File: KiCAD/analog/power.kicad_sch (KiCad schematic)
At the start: 0 parts

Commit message: KiCad revC: ±12V subsystem validated — LT1054 Fig-15 inverter + LM2940 LDO
Converged after iterating in LTspice:

* New standalone power project (KiCAD/power/) proves the topology before
  surgery on the analog project's power sheet. LT1054 as regulated inverter
  (not Figure 22 doubler — doubler was abandoned when single-FB-loop couldn't
  regulate both rails symmetrically). LM2940CT-12 LDO handles +12V from the
  13.8V bus. Both rails measure ±11.93V in sim at 1K load, VREF holds flat
  at 2.5V, V(FB_SD) settles at 0.596V.

* Datasheet-compliant divider values after discovering R16=10K violated the
  VREF ±100µA current limit: R16=20K, R17=240K (empirically tuned, differs
  from both my circuit analysis and datasheet formula — LTspice LT1054 model
  uses ~0.6V internal reference instead of the datasheet's 1.21V).
  C18=2.2nF loop comp matches datasheet "2 nF for all output voltages".

* New LM2940CT-12 symbol in xmitter.kicad_sym (TO-220-3, drop-in replacement
  for LM7812 pinout, 0.5V dropout vs 7812's 2V — needed for 13.8V-to-12V
  with headroom to spare).

* LTspice validation files in Documentation/:
    - power_sim.cir  (hand-written netlist, works in LTspice via File→Open)
    - power_sim.asc  (initial schematic attempt, retained as reference —
                      geometry is messy, use .cir instead)
    - Draft3.asc     (scratch for inspecting LT1054 symbol pin order)

Next step: migrate the validated topology into KiCAD/analog/power.kicad_sch,
replacing the shelved tube-era regulators (U15 LM317L, U19 LM7812, U23
LT1054) and the removed bridge rectifier that fed them.

Co-Authored-By: Claude Opus 4.7 <noreply@anthropic.com>
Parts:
- added C108: 220nF, Capacitor_THT:C_Disc_D6.0mm_W2.5mm_P5.00mm, symbol Device:C_US
- added C109: 0.47uF, Capacitor_THT:C_Rect_L7.0mm_W3.5mm_P5.00mm, symbol Device:C
- added C11: 10uF, symbol Device:C_Polarized_US
- added C110: 0.1uF, Capacitor_THT:C_Disc_D5.0mm_W2.5mm_P5.00mm, symbol Device:C
- added C111: 22uF, Capacitor_THT:CP_Radial_D5.0mm_P2.00mm, symbol Device:C_Polarized
- added C12: C_US, symbol Device:C_US
- added C13: 100uF, symbol Device:C_Polarized_US
- added C16: 0.001uF, symbol Device:C
- added J3: Screw_Terminal_01x02, symbol Connector:Screw_Terminal_01x02
- added R14: 10K, symbol Device:R_US
- added R15: 82K for -11.1V, 91K for -12.0V, symbol Device:R_US
- added U6: LT1054, symbol Regulator_SwitchedCapacitor:LT1054
- added U8: LM2940CT-12, Package_TO_SOT_THT:TO-220-3_Vertical, symbol xmitter:LM2940CT-12
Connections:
- new net: C108.1, C109.1, C12.1, J3.2 (Pin_2), U6.8 (V+), U8.1 (VI)
- new net: R14.1, U6.1 (FB/SHDN)
- new net: C16.2, R14.2, R15.1, U6.6 (VREF)
- new net: C11.1, U6.2 (CAP+)
- new net: C11.2, U6.4 (CAP-)
- new net +12V: C110.1, C111.1, U8.3 (VO)
- new net -12V: C13.2, C16.1, R15.2, U6.5 (-VOUT)
- new net GND: C108.2, C109.2, C110.2, C111.2, C12.2, C13.1, J3.1 (Pin_1), U6.3 (GND), U8.2 (GND)
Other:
- note added: "13.8V in"
- note added: "C105"

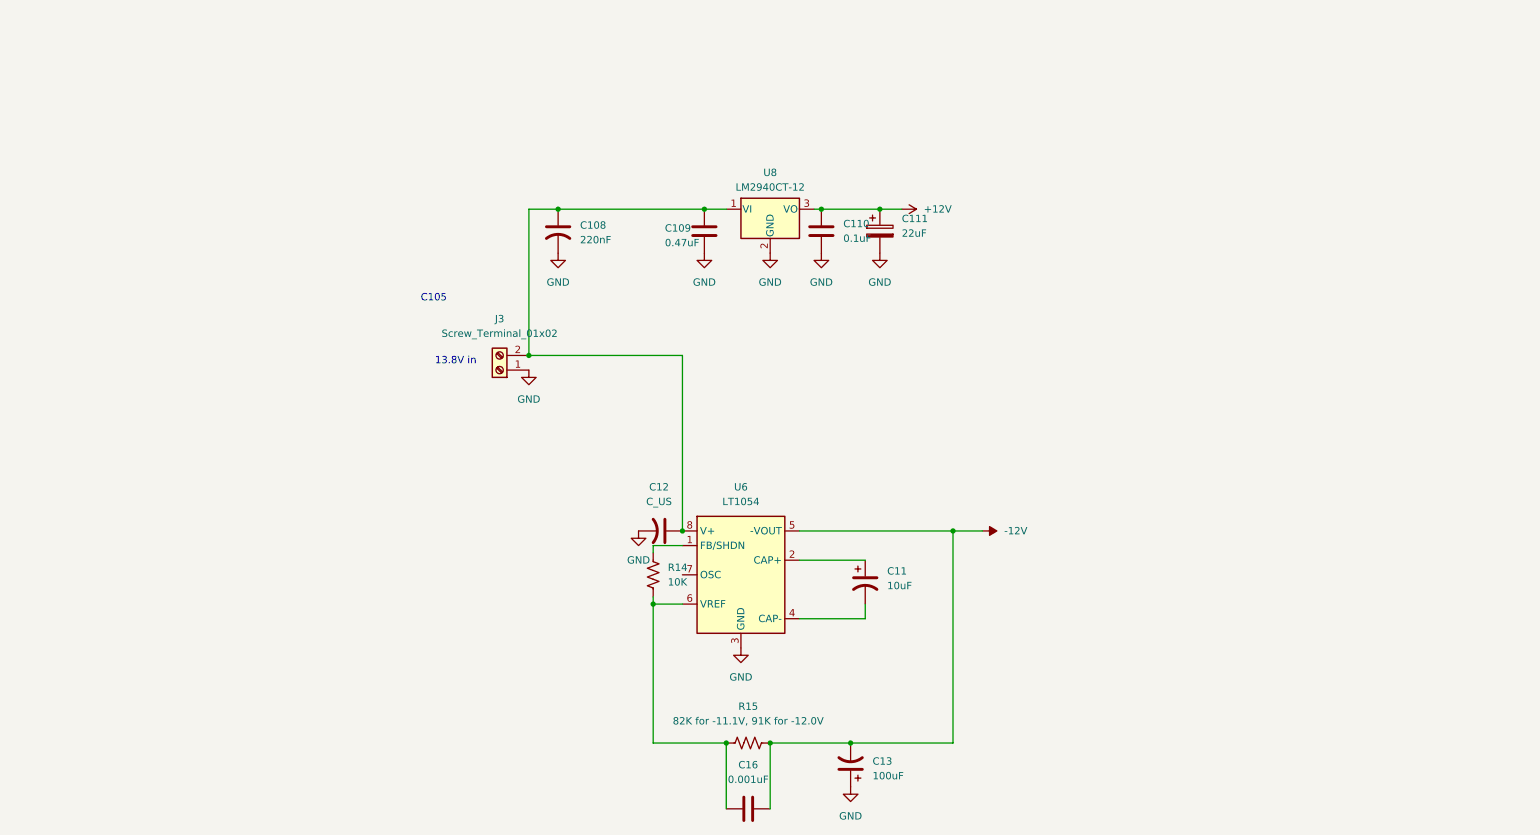
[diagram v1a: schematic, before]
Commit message: KiCad revC: LM2940CT-5.0 symbol + ±12V subsystem migrated into analog/power
* xmitter.kicad_sym: new LM2940CT-5.0 symbol, pin-compat with 7805 (same
  TO-220 topology as the LM2940CT-12 added last commit). For the +5V rail
  feeding the Metro.

* analog/power.kicad_sch: substantial migration of the validated ±12V
  subsystem (LT1054 regulated inverter + LM2940CT-12 LDO) from the
  standalone KiCAD/power/ project.  Tube-era regulators (LM317L, LM7812,
  original LT1054 attempt) and bridge rectifier gone. Values still need
  final cleanup (R14=10K->20K, R15 string->240K, C16=1n->2.2n, C12 no
  value) before next sim validation.

* Not pushing yet — 28V relay doubler stage will land in the same sheet
  before this gets published.

Co-Authored-By: Claude Opus 4.7 <noreply@anthropic.com>
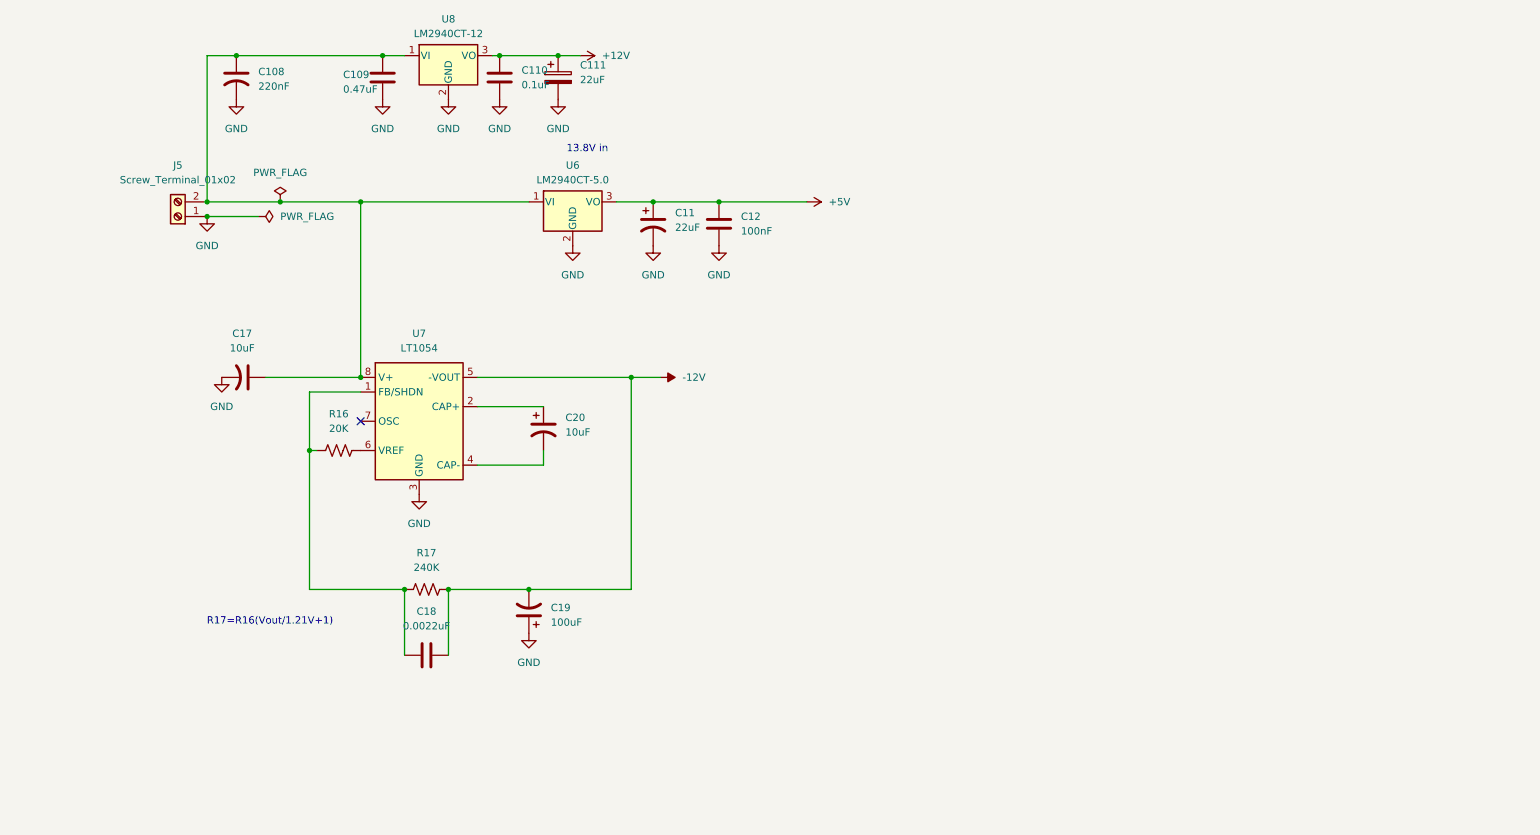
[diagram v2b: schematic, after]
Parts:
- removed C12: C_US, symbol Device:C_US
- removed C13: 100uF, symbol Device:C_Polarized_US
- removed C16: 0.001uF, symbol Device:C
- removed J3: Screw_Terminal_01x02, symbol Connector:Screw_Terminal_01x02
- removed R14: 10K, symbol Device:R_US
- removed R15: 82K for -11.1V, 91K for -12.0V, symbol Device:R_US
- removed U6: LT1054, symbol Regulator_SwitchedCapacitor:LT1054
- added C12: 100nF, symbol Device:C
- added C17: 10uF, symbol Device:C_US
- added C18: 0.0022uF, symbol Device:C
- added C19: 100uF, symbol Device:C_Polarized_US
- added C20: 10uF, symbol Device:C_Polarized_US
- added J5: Screw_Terminal_01x02, symbol Connector:Screw_Terminal_01x02
- added R16: 20K, symbol Device:R_US
- added R17: 240K, symbol Device:R_US
- added U6: LM2940CT-5.0, Package_TO_SOT_THT:TO-220-3_Vertical, symbol xmitter:LM2940CT-5.0
- added U7: LT1054, symbol Regulator_SwitchedCapacitor:LT1054
- C11: value 10uF -> 22uF
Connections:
- net -12V: now also C18.1, C19.2, R17.2, U7.5 (-VOUT)
- net GND: now also C11.2, C12.2, C17.2, C19.1, J5.1 (Pin_1), U6.2 (GND), U7.3 (GND)
- net at C108.1, C109.1, U8.1 (VI): now also C17.1, J5.2 (Pin_2), U6.1 (VI), U7.8 (V+)
- net +5V: now reaches C11.1
- net +5V: now also C12.1, U6.3 (VO)
- new net: C18.2, R16.1, R17.1, U7.1 (FB/SHDN)
- new net: C20.1, U7.2 (CAP+)
- new net: C20.2, U7.4 (CAP-)
- new net: R16.2, U7.6 (VREF)
- no-connect marks 0 -> 1
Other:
- note added: "R17=R16(Vout/1.21V+1)"
- note removed: "C105"

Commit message: KiCad revC: +28V doubler + 5V LDO added to analog/power, ERC clean
- Migrated LT1054 Figure 20 positive doubler from standalone power project
  into analog/power.kicad_sch for the +28V reed-relay rail
- Added LM2940CT-5.0 LDO stage for Metro / Si5351 +5V rail
- analog ERC: 4 messages, all classified as false positives (U9 pin 5
  tied to GND per Fig 20 topology, PCF_P5_SPARE intentionally unused,
  VIN pins now driven by added +5V rail)
- Added QRP Labs 10W PA / 5W PA reference PDFs + 2N7000 + lm2940c
  datasheets to Documentation/QRP_Examples/

Co-Authored-By: Claude Opus 4.7 <noreply@anthropic.com>
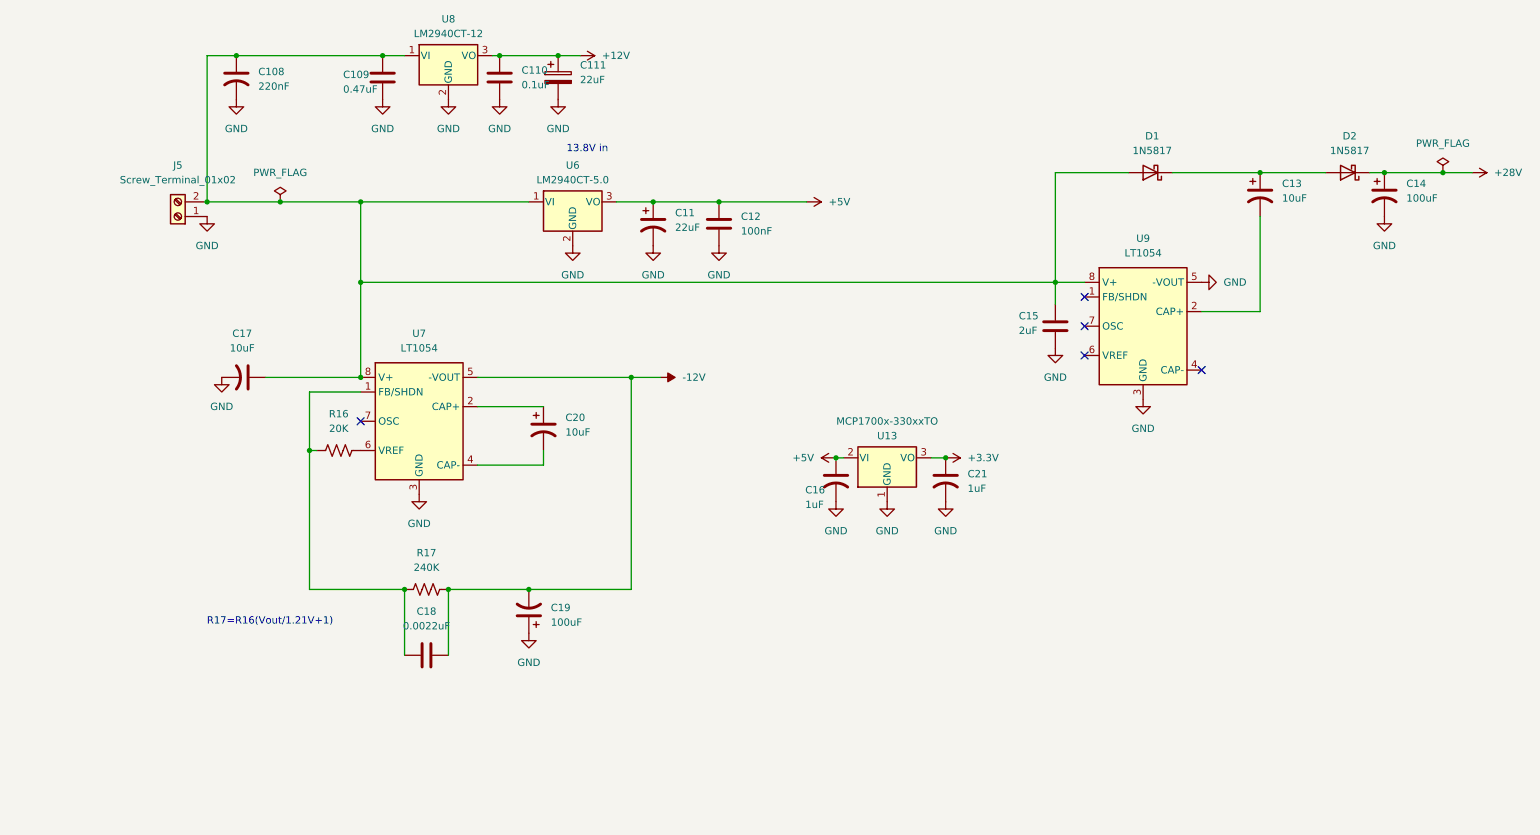
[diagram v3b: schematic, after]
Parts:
- added C13: 10uF, symbol Device:C_Polarized_US
- added C14: 100uF, symbol Device:C_Polarized_US
- added C15: 2uF, symbol Device:C
- added C16, C21: 1uF, Capacitor_THT:C_Rect_L7.2mm_W4.5mm_P5.00mm, symbol Device:C_US
- added D1, D2: 1N5817, Diode_THT:D_DO-41_SOD81_P10.16mm_Horizontal, symbol Diode:1N5817
- added U13: MCP1700x-330xxTO, Package_TO_SOT_THT:TO-92_Inline_Wide, symbol Regulator_Linear:MCP1700x-330xxTO
- added U9: LT1054, symbol Regulator_SwitchedCapacitor:LT1054
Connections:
- net +5V: now also C16.1, U13.2 (VI)
- net GND: now also C14.2, C15.2, C16.2, C21.2, U13.1 (GND), U9.3 (GND), U9.5 (-VOUT)
- net at C108.1, C109.1, C17.1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: now also C15.1, D1.2 (A), U9.8 (V+)
- new net: C13.1, D1.1 (K), D2.2 (A)
- new net: C13.2, U9.2 (CAP+)
- new net +28V: C14.1, D2.1 (K)
- new net +3.3V: C21.1, U13.3 (VO)
- no-connect marks 1 -> 5

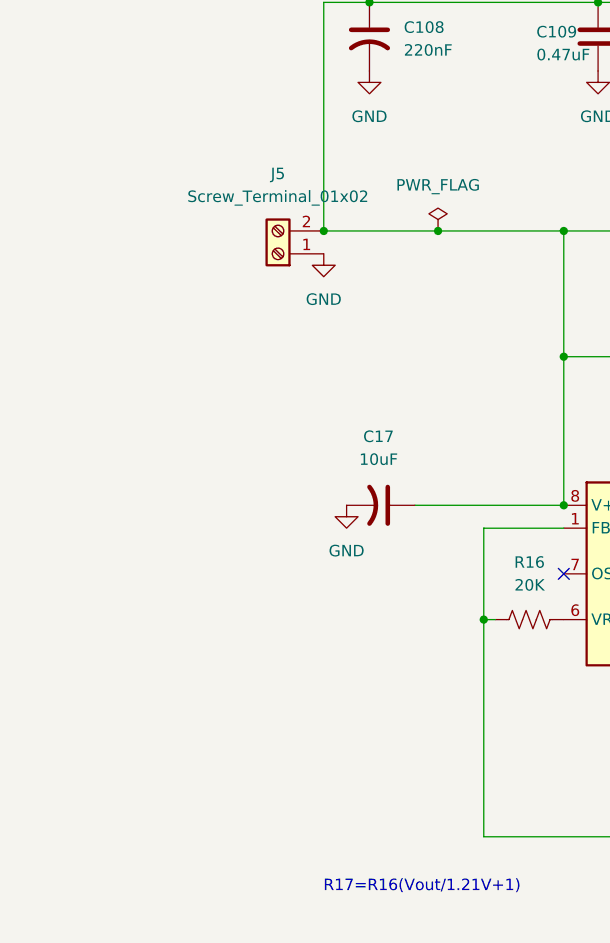
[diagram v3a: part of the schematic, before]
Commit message: KiCad revC: heartbeat-triggered SS PA power disconnect + flyback diodes
analog/power.kicad_sch:
- Added K6 (RLP20-12L10MS2F SPST-NO relay, 10A @ 30V DC contacts,
  12V/20mA coil) in series between +13.8V shack supply and J33
  (new 2-pin screw terminal supplying ss_pa board)
- K6 coil driven by existing Q5+Q7 series safety cascade on
  SS_PWR_RLY net: both Q5 (firmware control via PCF8575 P14) AND
  Q7 (CD14538B heartbeat watchdog Q_A) must be ON for the relay
  to energize. Firmware disable or heartbeat failure cuts PA power.
- Added 90R series resistor in the coil leg to drop +13.8V rail
  down to the 12V coil's nominal operating voltage
- Added D4 (1N4001 flyback diode) across K6 coil, cathode on +13.8V
  side, anode on SS_PWR_RLY (Q5 drain) side
- J7 (tube-era HV primary screw terminal) remains on the SS_PWR_RLY
  net so a future external tube-PA HV relay would share the same
  safety chain

ss_pa/pa_stage.kicad_sch:
- Added D2 (1N5822 Schottky, 3A/40V) flyback diode across L5. When
  the heartbeat relay opens with current flowing through L5, the
  12 uH inductor's stored energy (up to ~13 uJ at 1.5A) would
  otherwise swing the relay-side node hundreds of volts negative
  and arc the K6 contacts. D2 clamps that swing to ~V_f below the
  C6-held +13.8V bus.
- D2 polarity: cathode (pin 1) on J2/relay side, anode (pin 2) on
  +13.8V bus side.

Both netlists re-exported.

Co-Authored-By: Claude Opus 4.7 <noreply@anthropic.com>
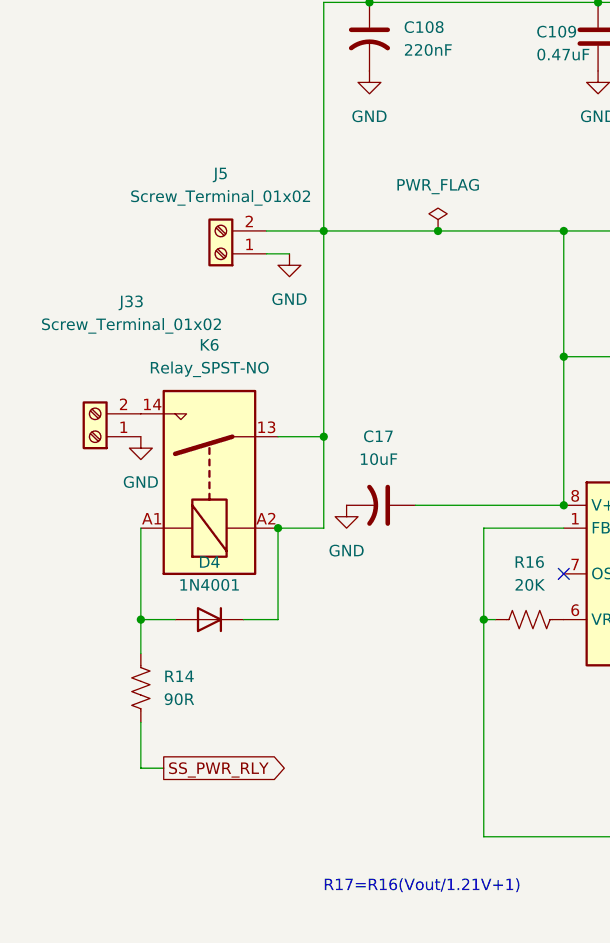
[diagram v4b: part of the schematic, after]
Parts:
- added D4: 1N4001, Diode_THT:D_DO-41_SOD81_P10.16mm_Horizontal, symbol Diode:1N4001
- added J33: Screw_Terminal_01x02, symbol Connector:Screw_Terminal_01x02
- added K6: Relay_SPST-NO, symbol Relay:Relay_SPST-NO
- added R14: 90R, symbol Device:R_US
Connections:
- net GND: now also J33.1 (Pin_1)
- net at C108.1, C109.1, C15.1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: now also D4.1 (K), K6.13, K6.A2
- new net: D4.2 (A), K6.A1, R14.1
- new net: J33.2 (Pin_2), K6.14
- new net SS_PWR_RLY: R14.2
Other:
- moved on the sheet: J5

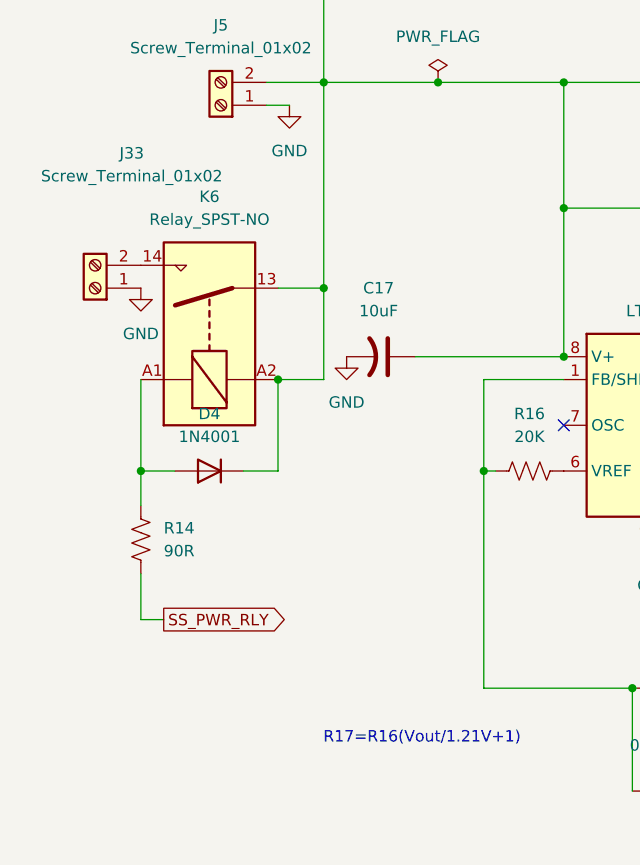
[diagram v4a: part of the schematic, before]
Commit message: KiCad revC: analog R6 -> 0R jumper (ENC_INT line)
Protoshield already has R7 (330R) + R8 (10K pullup) at the Metro
GPIO input, which is the right place for ESD/noise conditioning
(closest to the sensitive pin). R6 on analog was a duplicate series
resistor on the same signal; dropping it to 0R turns it into an
in-the-path jumper without having to rename the ENC_INT_CLEAN /
ENC_INT labels on multiple sheets.

Co-Authored-By: Claude Opus 4.7 <noreply@anthropic.com>
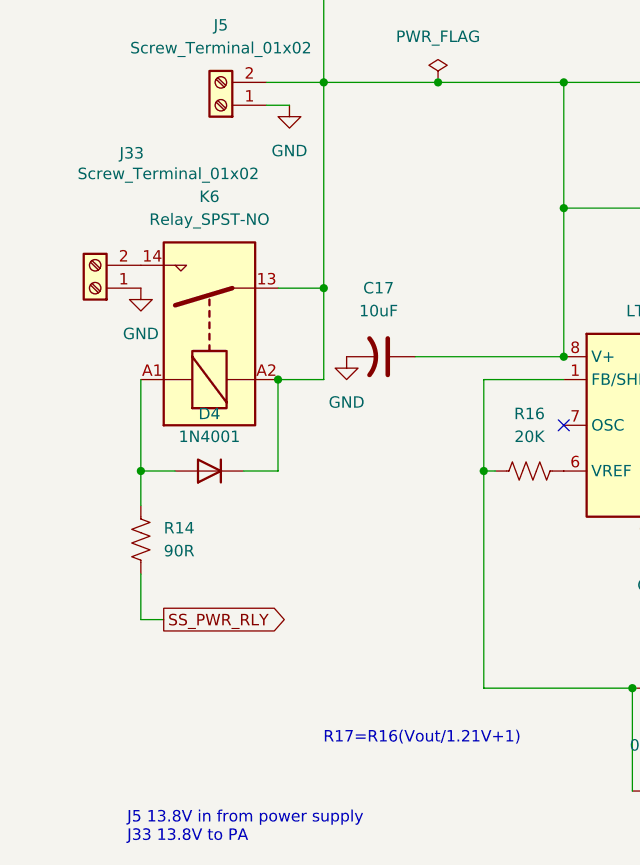
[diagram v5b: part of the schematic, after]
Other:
- note added: "J5 13.8V in from power supply J33 13.8V to PA"
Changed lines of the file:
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@@
+		)
+	)
+	(text "J5 13.8V in from power supply\nJ33 13.8V to PA"
+		(exclude_from_sim no)
+		(at 21.336 143.764 0)
+		(effects
+			(font
+				(size 1.27 1.27)
+			)
+			(justify left)
 		)
 	)
@@
 		)
 		(property "Value" "Screw_Terminal_01x02"
-			(at 21.844 71.374 0)
-			(show_name no)
-			(do_not_autoplace no)
+			(at 25.908 71.12 0)
+			(show_name no)
+			(do_not_autoplace no)
